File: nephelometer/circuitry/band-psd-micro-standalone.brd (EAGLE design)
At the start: 88 x 54 mm, 70 parts, among them IC1 LMC6484P, IC2 LM555N, IC3 74HCT74N, IC4 4044N, IC8 7805TV, J1 J5MM, T1 2N2222, T2 2N2222, U1 MAX4544, U4 MotA

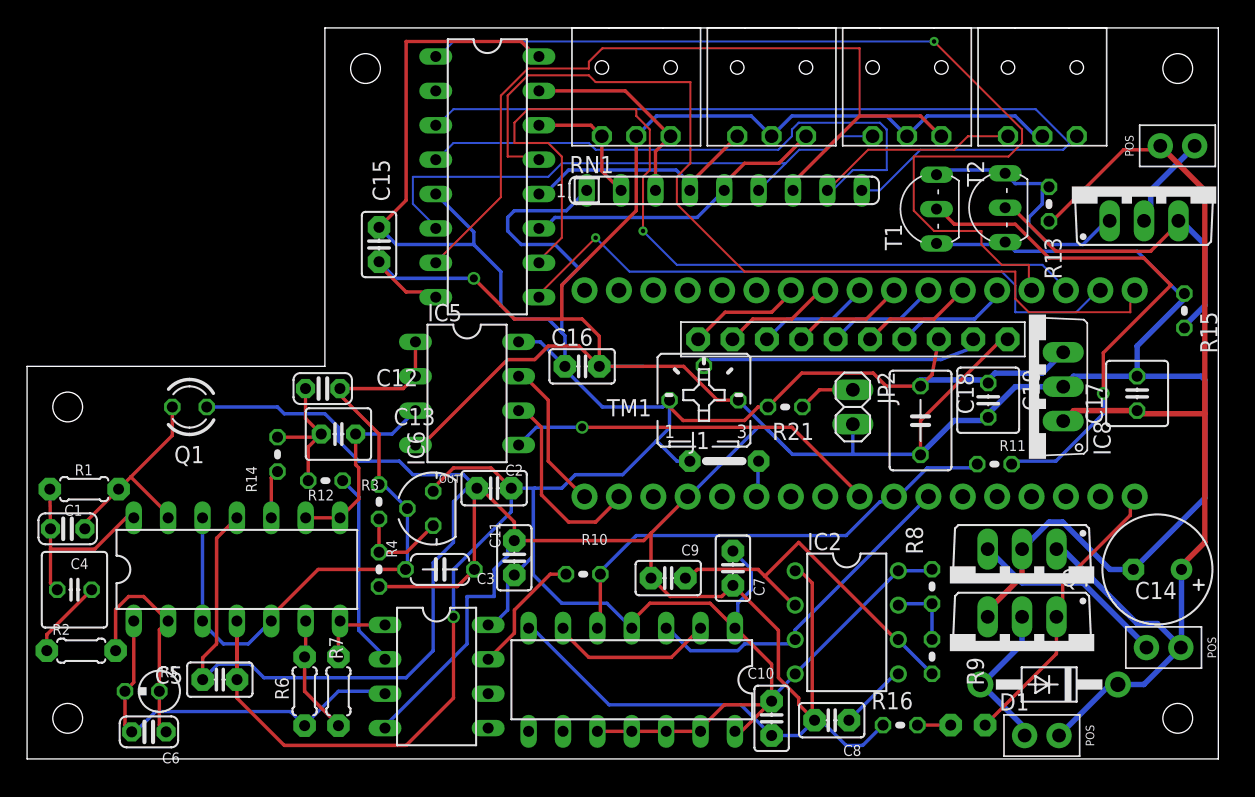
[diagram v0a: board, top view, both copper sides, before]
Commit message: Finished placement labels and added test point
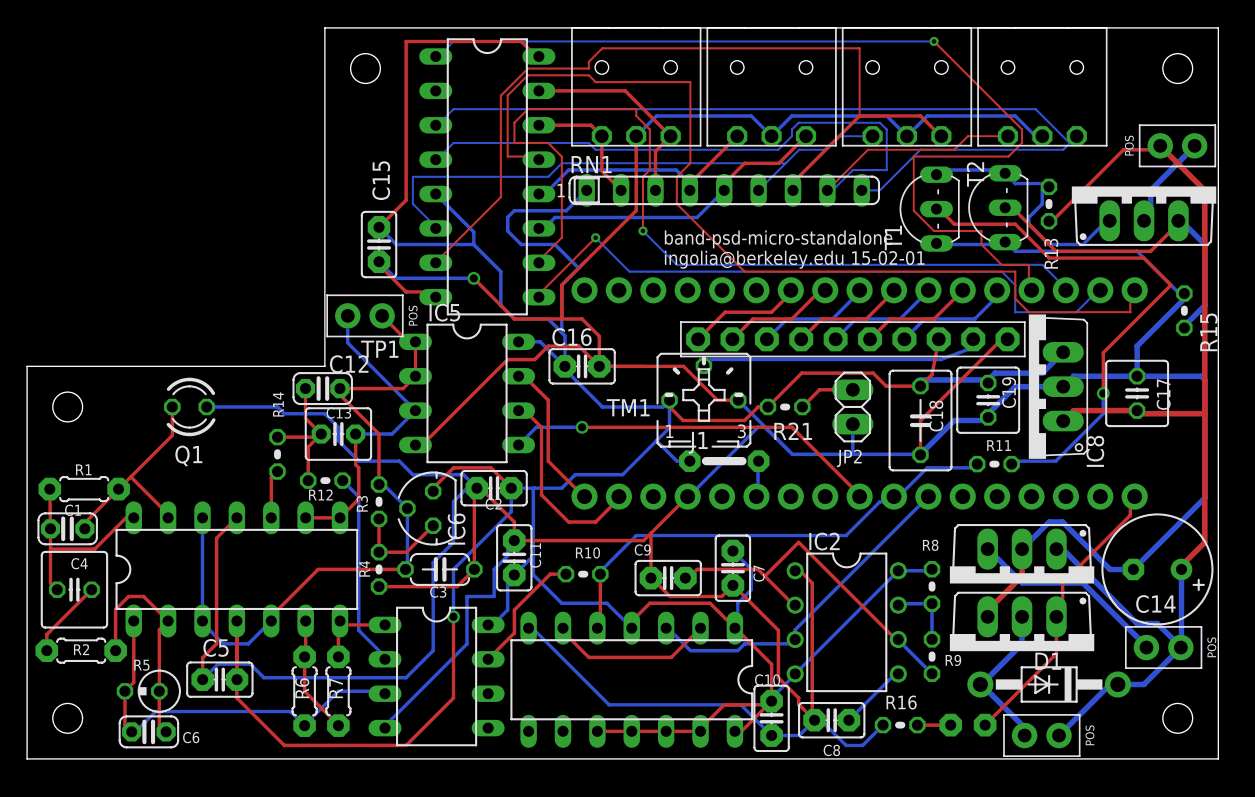
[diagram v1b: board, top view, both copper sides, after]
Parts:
- added TP1: (no value), ingolia:1X02_SCREW
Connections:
- net 2.5V: now also TP1.1/POS
- net N$28: now also TP1.2
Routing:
- net N$28: track 14.5 -> 23.6 mm
- net 2.5V: track 50.1 -> 53.3 mm
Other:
- board text added: "band-psd-micro-standalone ingolia@berkeley.edu 15-02-01"
- board text removed: "A+"
- board text removed: "K-"
- board text removed: "OUT"
- board text removed: "backlight"

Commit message: Finished BOM part assignments
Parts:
- R15: value 6.3R -> 6.2R
